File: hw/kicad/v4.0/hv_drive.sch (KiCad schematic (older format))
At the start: 21 parts, among them P6 CONN_01X02, P8 CONN_01X03, U12 IKCM20L60GD

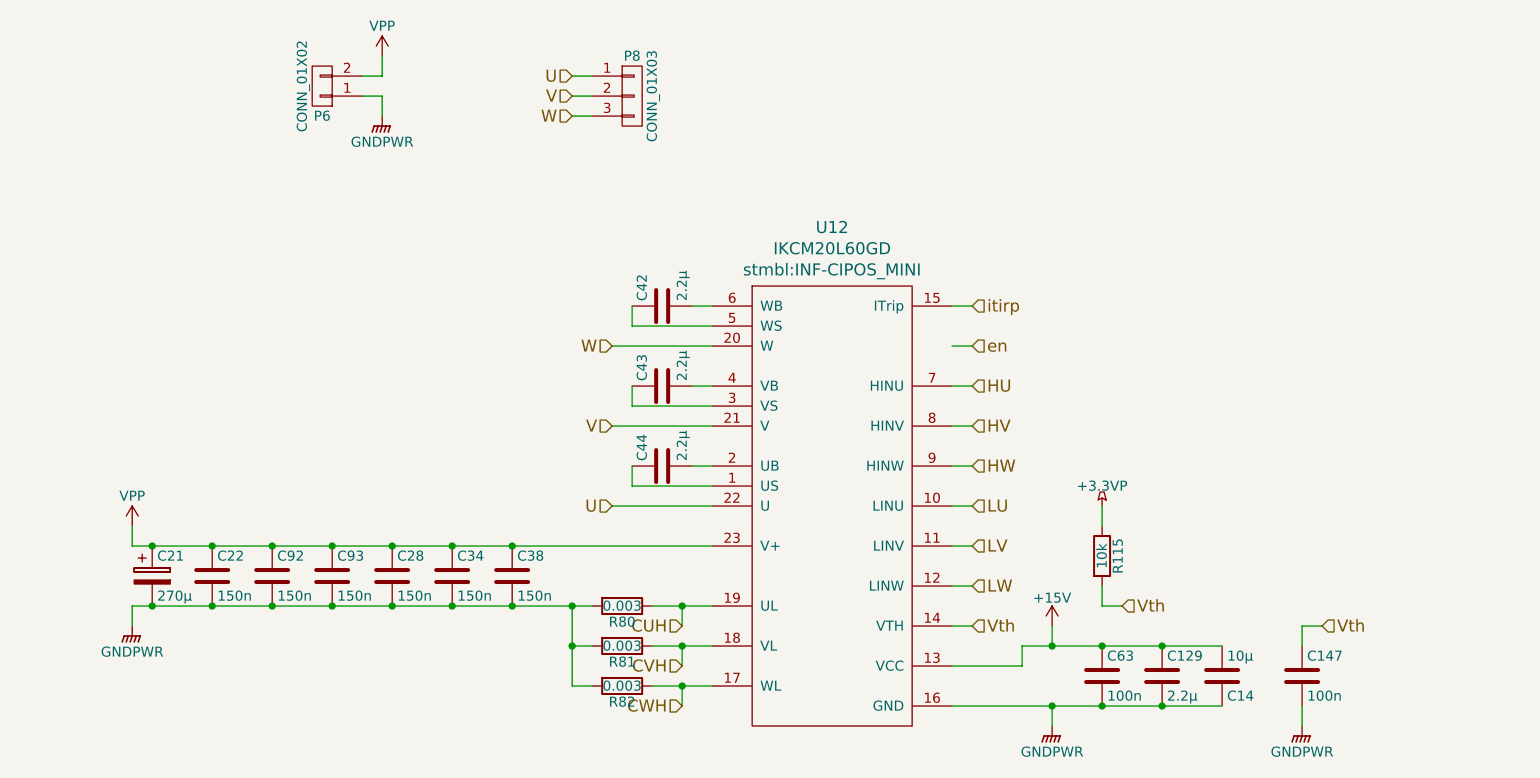
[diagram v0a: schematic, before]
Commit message: changes for IKCM30F60GD
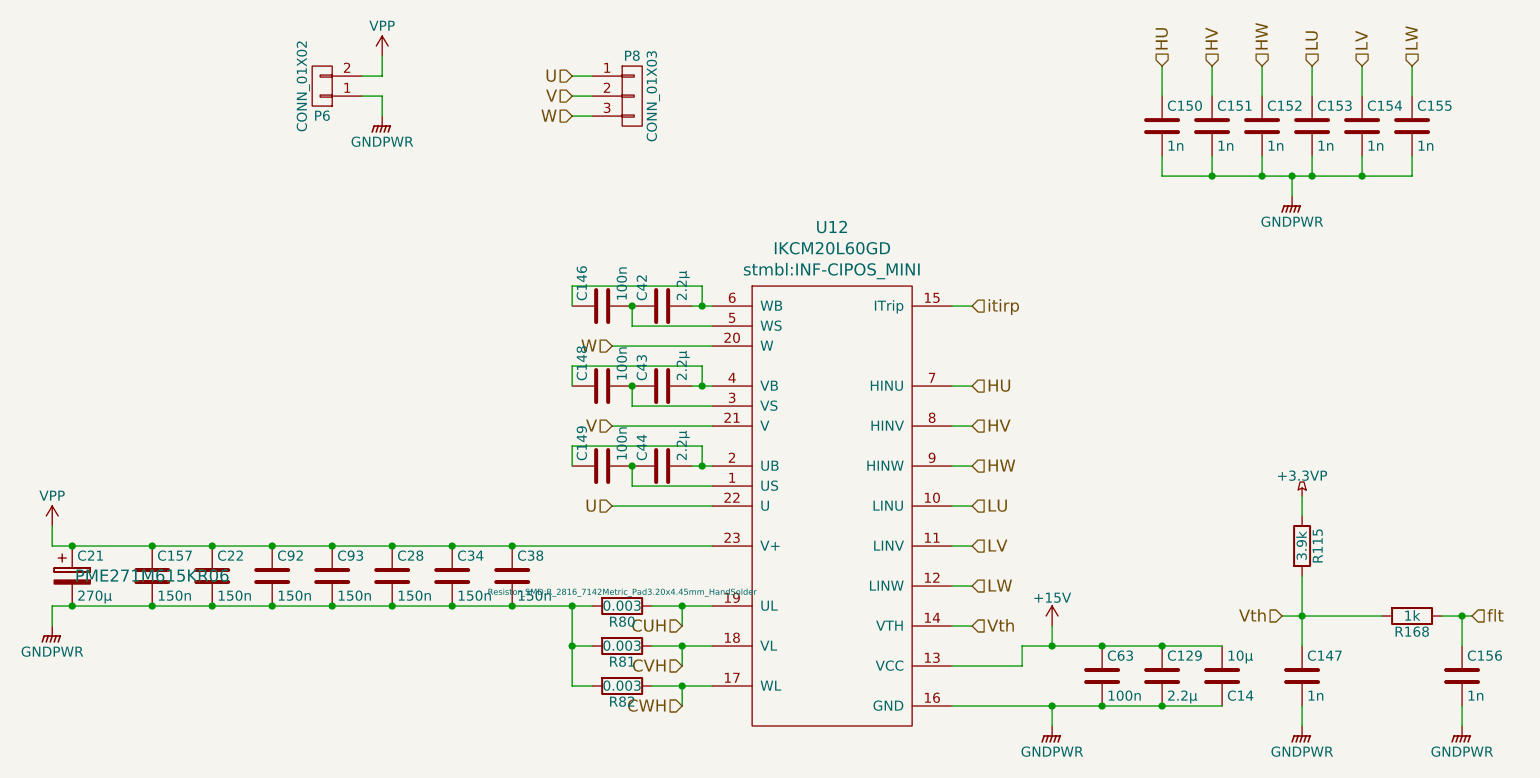
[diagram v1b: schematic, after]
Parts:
- added C146, C148, C149: 100n, stmbl:C_0603, symbol stmbl:C
- added C150, C151, C152, C153, C154, C155, C156: 1n, stmbl:C_0603, symbol stmbl:C
- added C157: 150n, stmbl:C_Rect_L24.0mm_W10.1mm_P22.50mm_MKT, symbol stmbl:C
- added R168: 1k, stmbl:R_0603, symbol stmbl:R
- C147: value 100n -> 1n
- R115: value 10k -> 3.9k
- R80, R81: footprint stmbl:R_2512 -> Resistor_SMD:R_2816_7142Metric_Pad3.20x4.45mm_HandSolder
- R82: footprint stmbl:R_2512 -> Resistor_SMD:R_2816_7142Metric_Pad3.20x4.45mm_HandSolder; Manufacturer No CSS2H-2512K-3L00F -> WSHM28186L000FEA
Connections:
- net GNDPWR: now also C150.2, C151.2, C152.2, C153.2, C154.2, C155.2, C156.2, C157.2
- net HU: now also C150.1
- net HV: now also C151.1
- net HW: now also C152.1
- net LU: now also C153.1
- net LV: now also C154.1
- net LW: now also C155.1
- net VPP: now also C157.1
- net Vth: now also R168.2
- net at C42.1, U12.5 (WS): now also C146.2
- net at C42.2, U12.6 (WB): now also C146.1
- net at C43.1, U12.3 (VS): now also C148.2
- net at C43.2, U12.4 (VB): now also C148.1
- net at C44.1, U12.1 (US): now also C149.2
- net at C44.2, U12.2 (UB): now also C149.1
- new net flt: C156.1, R168.1
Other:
- moved on the sheet: C21, R115
